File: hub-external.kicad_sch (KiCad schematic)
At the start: 45 parts, among them J2 USB-C 5V POWER, U23 TLV75533PDBVR, U25 SN74LVC1G02DBVR, U27 TPS22975DSGR, U28 TPS552892RYQR, U46 INA300AIDGSR, U7 TUSB320LAIRWBR

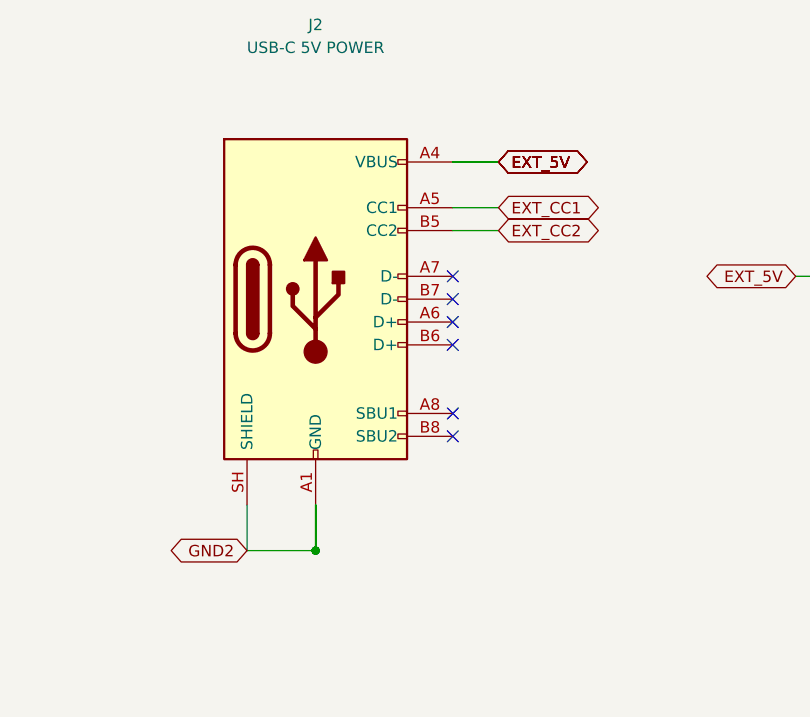
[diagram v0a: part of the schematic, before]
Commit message: feat(revc): assign exact BOM and verified local land patterns
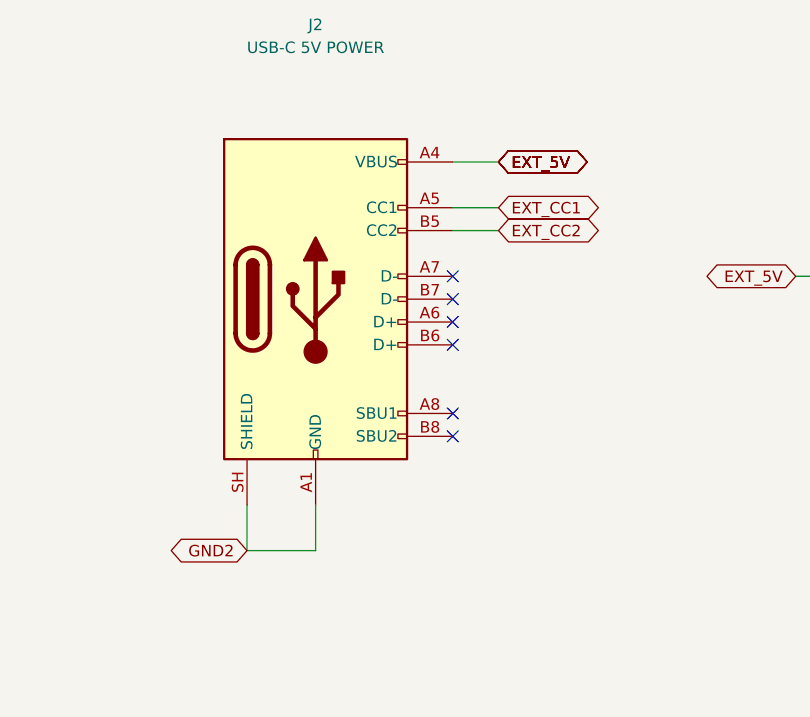
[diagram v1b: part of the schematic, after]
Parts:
- C110, C23, C25, C26, C81, C82, C83, C89: footprint (none) -> hub-lib:C_0402_1005Metric; LCSC (none) -> C77020; MPN (none) -> GRM155R71H104KE14D; Manufacturer (none) -> Murata Manufacturing; Ratings (none) -> 50V X7R 10%
- C24, C77: footprint (none) -> hub-lib:C_0603_1608Metric; LCSC (none) -> C77046; MPN (none) -> GRM188R61E105KA12D; Manufacturer (none) -> Murata Manufacturing; Ratings (none) -> 25V X5R 10%
- C78: footprint (none) -> hub-lib:C_0402_1005Metric; LCSC (none) -> C77019; MPN (none) -> GRM155R71H103KA88D; Manufacturer (none) -> Murata Manufacturing; Ratings (none) -> 50V X7R 10%
- C79, C80, C85, C86, C87, C88: footprint (none) -> hub-lib:C_1210_3225Metric; LCSC (none) -> C21397; MPN (none) -> GRM32ER71E226KE15L; Manufacturer (none) -> Murata Manufacturing; Ratings (none) -> 25V X7R 10%
- C84: footprint (none) -> hub-lib:C_0805_2012Metric; LCSC (none) -> C84416; MPN (none) -> GRM21BR61E106KA73L; Manufacturer (none) -> Murata Manufacturing; Ratings (none) -> 25V X5R 10%
- C90: footprint (none) -> hub-lib:C_0402_1005Metric; LCSC (none) -> C77011; MPN (none) -> GRM155R71C224KA12D; Manufacturer (none) -> Murata Manufacturing; Ratings (none) -> 16V X7R 10%
- C91: footprint (none) -> hub-lib:C_0402_1005Metric; LCSC (none) -> C77177; MPN (none) -> GRM1555C1H101JA01D; Manufacturer (none) -> Murata Manufacturing; Ratings (none) -> 50V C0G 5%
- D5: footprint Diode_SMD:D_SOD-523 -> hub-lib:D_SOD-523; LCSC (none) -> C19950551; Ratings (none) -> See exact manufacturer datasheet
- J2: footprint Connector_USB:USB_C_Receptacle_HRO_TYPE-C-31-M-12 -> hub-lib:USB_C_Receptacle_HRO_TYPE-C-31-M-12; LCSC (none) -> C165948; Ratings (none) -> See exact manufacturer datasheet
- L3: footprint (none) -> hub-lib:L_Coilcraft_XAL7070-XXX; LCSC (none) -> C3911513; Ratings (none) -> See exact manufacturer datasheet
- R110: footprint (none) -> hub-lib:R_1206_3216Metric; LCSC (none) -> C441558; MPN (none) -> WSLP1206R0200FEA; Manufacturer (none) -> Vishay; Ratings (none) -> 1W, 1%, 75ppm/C; Kelvin sense
- R111: footprint (none) -> hub-lib:R_0603_1608Metric; LCSC (none) -> C861305; MPN (none) -> RT0603BRD072K87L; Manufacturer (none) -> Yageo; Ratings (none) -> 0.1%, 25ppm/C thin film, 0.1W
- R112: footprint (none) -> hub-lib:R_0402_1005Metric; LCSC (none) -> C242160; MPN (none) -> ERJ2GE0R00X; Manufacturer (none) -> Panasonic Industry; Ratings (none) -> 0R jumper, 0402, 1A rated current
- R16: footprint (none) -> hub-lib:R_0402_1005Metric; LCSC (none) -> C2085054; MPN (none) -> ERJ2RKF9093X; Manufacturer (none) -> Panasonic Industry; Ratings (none) -> 1%, 0.1W, 50V
- R17, R18, R61: footprint (none) -> hub-lib:R_0402_1005Metric; LCSC (none) -> C191123; MPN (none) -> ERJ2RKF1002X; Manufacturer (none) -> Panasonic Industry; Ratings (none) -> 1%, 0.1W, 50V
- R19: footprint (none) -> hub-lib:R_0402_1005Metric; LCSC (none) -> C192169; MPN (none) -> ERJ2RKF1003X; Manufacturer (none) -> Panasonic Industry; Ratings (none) -> 1%, 0.1W, 50V
- R20: footprint (none) -> hub-lib:R_0603_1608Metric; LCSC (none) -> C860067; MPN (none) -> RT0603BRB0710KL; Manufacturer (none) -> Yageo; Ratings (none) -> 0.1%, 10ppm/C thin film, 0.1W
- R21: footprint (none) -> hub-lib:R_0603_1608Metric; LCSC (none) -> C860379; MPN (none) -> RT0603BRB073KL; Manufacturer (none) -> Yageo; Ratings (none) -> 0.1%, 10ppm/C thin film, 0.1W
- R22: footprint (none) -> hub-lib:R_0603_1608Metric; LCSC (none) -> C860136; MPN (none) -> RT0603BRB0715RL; Manufacturer (none) -> Yageo; Ratings (none) -> 0.1%, 10ppm/C thin film, 0.1W
- R59: footprint (none) -> hub-lib:R_0402_1005Metric; LCSC (none) -> C409918; MPN (none) -> ERJ2RKF4992X; Manufacturer (none) -> Panasonic Industry; Ratings (none) -> 1%, 0.1W, 50V
- R60: footprint (none) -> hub-lib:R_0402_1005Metric; LCSC (none) -> C413089; MPN (none) -> ERJ2RKF2701X; Manufacturer (none) -> Panasonic Industry; Ratings (none) -> 1%, 0.1W, 50V
- TP17, TP7, TP8: footprint TestPoint:TestPoint_Pad_D1.0mm -> hub-lib:TestPoint_Pad_D1.0mm; Manufacturer (none) -> PCB feature; Ratings (none) -> Exposed test pad; no purchased part; now left out of the parts list
- U23: footprint (none) -> hub-lib:SOT-23-5; LCSC (none) -> C404027; Ratings (none) -> See exact manufacturer datasheet
- U25: footprint (none) -> hub-lib:SOT-23-5; LCSC (none) -> C16360; Ratings (none) -> See exact manufacturer datasheet
- U27: footprint (none) -> hub-lib:Texas_DSG0008A_WSON-8-1EP_2x2mm_P0.5mm_EP0.9x1.6mm; LCSC (none) -> C524777; Ratings (none) -> See exact manufacturer datasheet
- U28: footprint (none) -> hub-lib:TI_RYQ0021A_VQFN21_3x5mm; LCSC (none) -> C19272254; Ratings (none) -> See exact manufacturer datasheet
- U46: footprint (none) -> hub-lib:MSOP-10_3x3mm_P0.5mm; LCSC (none) -> C529558; Ratings (none) -> See exact manufacturer datasheet
- U7: footprint (none) -> hub-lib:Texas_X2QFN-12_1.6x1.6mm_P0.4mm; LCSC (none) -> C132554; Ratings (none) -> See exact manufacturer datasheet

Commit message: feat(revc): place synchronized unrouted board and correct bus startup
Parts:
- R22: value 15R -> 0R; footprint hub-lib:R_0603_1608Metric -> hub-lib:R_0402_1005Metric; LCSC C860136 -> C242160; MPN RT0603BRB0715RL -> ERJ2GE0R00X; Manufacturer Yageo -> Panasonic Industry; Ratings 0.1%, 10ppm/C thin film, 0.1W -> 0R jumper, 0402, 1A rated current
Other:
- note added: "Buck-boost power stage"
- note added: "Declared power origins"
- note added: "External source must advertise 3 A"
- note added: "Input inrush and port-shedding current monitor"
- note added: "Output setpoint and voltage-loop compensation"
- note added: "Power-only USB-C connector and 3.3 V bias"
- note added: "USB 2.0 / 480 Mbps | Rev C electrical design | Placement and routing review pending"
- note removed: "Rev C | all routing reserved for Alex | electrical draft under review"
- moved on the sheet: C110, C23, C24, C25, C26, C77, C78, C79, C80, C81, C82, C83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

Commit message: feat(revc): finish verified TI hub routing handoff
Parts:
- C84: value 10uF -> 22uF; footprint hub-lib:C_0805_2012Metric -> hub-lib:C_1210_3225Metric; LCSC C84416 -> C21397; MPN GRM21BR61E106KA73L -> GRM32ER71E226KE15L; Ratings 25V X5R 10% -> 25V X7R 10%
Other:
- note added: "USB 2.0 / 480 Mbps | Rev C electrical design | Placed PCB; all routing by Alex; hardware tests pending"
- note removed: "USB 2.0 / 480 Mbps | Rev C electrical design | Placement and routing review pending"
- moved on the sheet: D5
